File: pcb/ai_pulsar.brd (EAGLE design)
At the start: 30.5 x 30.5 mm, 24 parts, among them IC1 DS1307SO8-TIGHT, IC3 74HCT245MTC, J2 1X05, U1 MIC5205-3.3

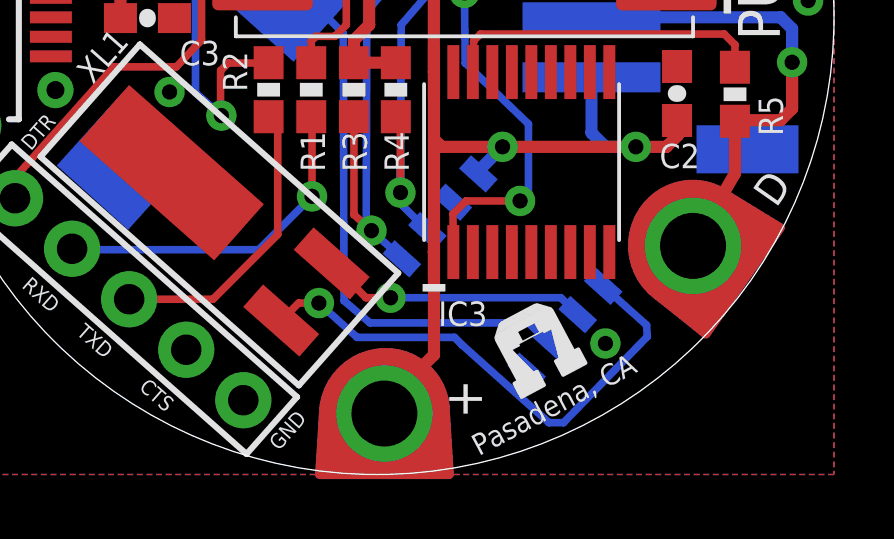
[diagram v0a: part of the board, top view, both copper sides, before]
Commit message: renamed a few parts
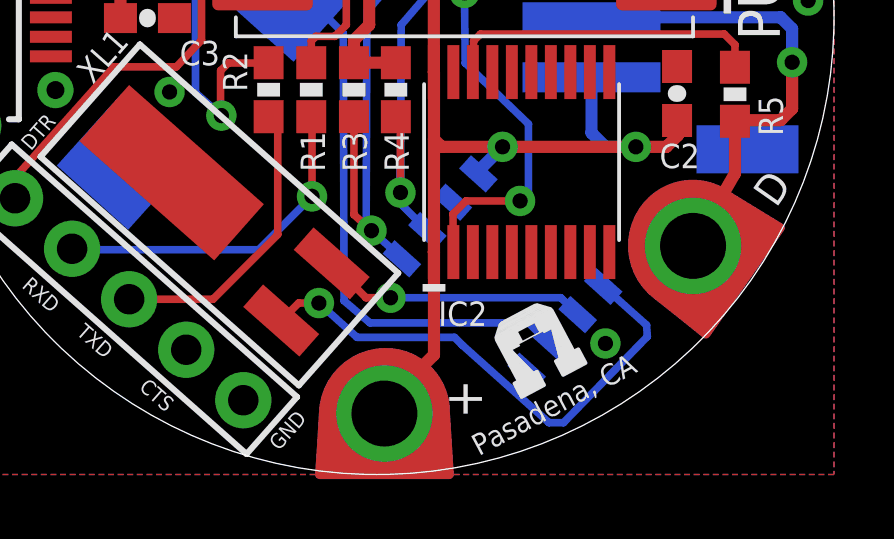
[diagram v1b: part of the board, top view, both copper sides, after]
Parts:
- C1: value 0.01uF -> 0.1uF
- renumbered IC3 to IC2
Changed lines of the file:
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@@
 <?xml version="1.0" encoding="utf-8"?>
 <!DOCTYPE eagle SYSTEM "eagle.dtd">
-<eagle version="7.1.0">
+<eagle version="7.0.0">
 <drawing>
 <settings>
@@
 <attribute name="NAME" x="10.1092" y="14.097" size="0.8128" layer="25" font="vector" ratio="10" rot="R270"/>
 </element>
-<element name="C1" library="Ai_Passives" package="CAP-0603" value="0.01uF" x="7.5946" y="18.0086" smashed="yes">
+<element name="C1" library="Ai_Passives" package="CAP-0603" value="0.1uF" x="7.5946" y="18.0086" smashed="yes">
 <attribute name="NAME" x="6.9596" y="18.7706" size="0.8128" layer="25" font="vector" ratio="10"/>
 </element>
-<element name="IC3" library="Ai_IC" package="SSOP20" value="74HCT245MTC" x="20.066" y="10.414" smashed="yes">
+<element name="IC2" library="Ai_IC" package="SSOP20" value="74HCT245MTC" x="20.066" y="10.414" smashed="yes">
 <attribute name="NAME" x="18.923" y="5.7658" size="0.8128" layer="25" font="vector" ratio="10" rot="R180"/>
 </element>
@@
 <contactref element="RFDUINO" pad="2"/>
 <contactref element="RFDUINO" pad="8"/>
-<contactref element="IC3" pad="10"/>
-<contactref element="IC3" pad="19"/>
+<contactref element="IC2" pad="10"/>
+<contactref element="IC2" pad="19"/>
 <contactref element="USB1" pad="GND"/>
 <contactref element="U1" pad="2"/>
@@
 <contactref element="+" pad="1"/>
 <contactref element="C2" pad="1"/>
-<contactref element="IC3" pad="20"/>
-<contactref element="IC3" pad="1"/>
+<contactref element="IC2" pad="20"/>
+<contactref element="IC2" pad="1"/>
 <contactref element="U1" pad="1"/>
 <contactref element="U1" pad="3"/>
@@
 <signal name="3V3IO2">
 <contactref element="RFDUINO" pad="3"/>
-<contactref element="IC3" pad="2"/>
+<contactref element="IC2" pad="2"/>
 <wire x1="17.791" y1="7.414" x2="17.78" y2="7.425" width="0.254" layer="1"/>
 <wire x1="17.78" y1="7.425" x2="17.78" y2="8.6868" width="0.254" layer="1"/>
@@
 </signal>
 <signal name="5VIO2">
-<contactref element="IC3" pad="18"/>
+<contactref element="IC2" pad="18"/>
 <contactref element="R5" pad="2"/>
 <wire x1="18.441" y1="13.414" x2="18.4658" y2="13.4388" width="0.254" layer="1"/>

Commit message: version 1.1. Fixed coin-cell polarity, added 5V on FTDI pins for easy programming
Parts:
- J1: value (none) -> JST-3-MALE; device Ai_Connectors:JSTP-3P-SMD -> Ai_Connectors:JST-3P-SMD
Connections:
- removed net CTS: J2.2
- removed net N$2: 3V-BATT.-, IC1.3
- new net N$1: 3V-BATT.+@1, 3V-BATT.+@2, IC1.3
- net 5V: now also J2.2
- net GND: now also 3V-BATT.-; no longer 3V-BATT.+$1, 3V-BATT.+$2
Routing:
- net N$2: track 18.9 -> 0.00 mm
- net N$1: track 0.00 -> 18.8 mm
- net 5V: track 49.5 -> 57.3 mm
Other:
- board text added: "5V"
- board text added: "v1.1"
- board text removed: "CTS"
- board text removed: "v1.0"
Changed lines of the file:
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@@
 <?xml version="1.0" encoding="utf-8"?>
 <!DOCTYPE eagle SYSTEM "eagle.dtd">
-<eagle version="7.0.0">
+<eagle version="7.1.0">
 <drawing>
 <settings>
@@
 <setting verticaltext="up"/>
 </settings>
-<grid distance="10" unitdist="mil" unit="mil" style="lines" multiple="1" display="yes" altdistance="0.025" altunitdist="inch" altunit="inch"/>
+<grid distance="5" unitdist="mil" unit="mil" style="lines" multiple="1" display="yes" altdistance="0.025" altunitdist="inch" altunit="inch"/>
 <layers>
 <layer number="1" name="Top" color="4" fill="1" visible="yes" active="yes"/>
@@
 <text x="17.653" y="3.175" size="1.27" layer="25" font="vector" ratio="10" rot="SR270">+</text>
 <text x="9.271" y="28.956" size="1.27" layer="25" font="vector" ratio="10" rot="SR180">-</text>
-<text x="29.8704" y="16.6624" size="0.7112" layer="25" font="vector" ratio="10" rot="R90">v1.0</text>
-<text x="3.7084" y="10.7696" size="0.508" layer="25" font="vector" ratio="10" rot="R48.5">DTR</text>
-<text x="4.7244" y="5.7404" size="0.508" layer="25" font="vector" ratio="10" rot="R138.5">RXD</text>
-<text x="6.5024" y="4.2164" size="0.508" layer="25" font="vector" ratio="10" rot="R138.5">TXD</text>
-<text x="8.5344" y="2.4384" size="0.508" layer="25" font="vector" ratio="10" rot="R138.5">CTS</text>
-<text x="12.5476" y="2.1844" size="0.508" layer="25" font="vector" ratio="10" rot="R228.5">GND</text>
+<text x="29.8704" y="16.6624" size="0.7112" layer="25" font="vector" ratio="10" rot="R90">v1.1</text>
+<text x="3.8354" y="10.5156" size="0.762" layer="25" font="vector" ratio="10" rot="R48.5">DTR</text>
+<text x="5.1054" y="5.4864" size="0.762" layer="25" font="vector" ratio="10" rot="R138.5">RXD</text>
+<text x="7.0104" y="3.8354" size="0.762" layer="25" font="vector" ratio="10" rot="R138.5">TXD</text>
+<text x="8.2804" y="2.6924" size="0.762" layer="25" font="vector" ratio="10" rot="R138.5">5V</text>
+<text x="12.8016" y="2.4384" size="0.762" layer="25" font="vector" ratio="10" rot="R228.5">GND</text>
 </plain>
 <attributes>
@@
 <attribute name="NAME" x="18.923" y="5.7658" size="0.8128" layer="25" font="vector" ratio="10" rot="R180"/>
 </element>
-<element name="3V-BATT" library="Ai_Connectors" package="CR1220-SMD" value="CR1220" x="12.319" y="16.51" smashed="yes" rot="MR312"/>
 <element name="IC1" library="Ai_IC" package="SO08-TIGHT" value="DS1307SO8-TIGHT" x="19.431" y="6.731" smashed="yes" rot="MR312">
 <attribute name="NAME" x="22.70684375" y="7.712009375" size="0.8128" layer="26" ratio="10" rot="MR42"/>
 </element>
-<element name="J1" library="Ai_Connectors" package="JSTP-3P-SMD" value="" x="25.0952" y="15.24" smashed="yes" rot="MR90"/>
+<element name="J1" library="Ai_Connectors" package="JST-3P-SMD" value="JST-3-MALE" x="25.0952" y="15.24" smashed="yes" rot="MR90"/>
 <element name="-" library="Ai_Connectors" package="1X01-PETAL" value="1X01-PETAL" x="6.985" y="25.4" smashed="yes" rot="R40"/>
 <element name="+" library="Ai_Connectors" package="1X01-PETAL" value="1X01-PETAL" x="15.494" y="2.032" smashed="yes" rot="R180"/>
@@
 <attribute name="NAME" x="7.62" y="20.32" size="0.8128" layer="25" font="vector" ratio="10" rot="R150"/>
 </element>
+<element name="3V-BATT" library="Ai_Connectors" package="CR1220-SMD" value="CR1220" x="12.319" y="16.51" smashed="yes" rot="MR312"/>
 </elements>
 <signals>
@@
 <contactref element="U1" pad="2"/>
 <contactref element="J1" pad="3"/>
-<contactref element="3V-BATT" pad="+$1"/>
-<contactref element="3V-BATT" pad="+$2"/>
 <contactref element="J2" pad="1"/>
 <contactref element="IC1" pad="4"/>
@@
 <via x="8.3312" y="12.7508" extent="1-16" drill="0.508"/>
 <via x="22.86" y="4.3688" extent="1-16" drill="0.508"/>
+<contactref element="3V-BATT" pad="-"/>
 </signal>
 <signal name="N$9">
@@
 <wire x1="16.002" y1="19.9136" x2="17.141" y2="18.7746" width="0.4064" layer="1"/>
 <wire x1="17.141" y1="18.7746" x2="17.141" y2="13.414" width="0.4064" layer="1"/>
+<contactref element="J2" pad="2"/>
+<wire x1="8.887346875" y1="4.15894375" x2="12.192" y2="4.953" width="0.4064" layer="16"/>
+<wire x1="12.192" y1="4.953" x2="15.494" y2="2.032" width="0.4064" layer="16"/>
 </signal>
 <signal name="3V3" class="1">
@@
 <wire x1="27.2144" y1="11.811" x2="27.178" y2="11.7746" width="0.4064" layer="1"/>
 </signal>
-<signal name="N$2">
-<contactref element="IC1" pad="3"/>
-<contactref element="3V-BATT" pad="-"/>
-<wire x1="12.319" y1="16.51" x2="14.1224" y2="14.7066" width="0.254" layer="16"/>
-<wire x1="14.1224" y1="14.7066" x2="14.1478" y2="5.7912" width="0.254" layer="16"/>
-<wire x1="14.1478" y1="5.7912" x2="15.0114" y2="5.0546" width="0.254" layer="16"/>
-<wire x1="15.0114" y1="5.0546" x2="20.2946" y2="5.0546" width="0.254" layer="16"/>
-<wire x1="20.2946" y1="5.0546" x2="20.989065625" y2="4.385534375" width="0.254" layer="16"/>
-<wire x1="20.989065625" y1="4.385534375" x2="21.086909375" y2="4.385534375" width="0.254" layer="16"/>
-</signal>
-<signal name="CTS">
-<contactref element="J2" pad="2"/>
-</signal>
 <signal name="TXO">
 <contactref element="J2" pad="3"/>
@@
 <wire x1="6.8009125" y1="21.569" x2="6.477" y2="21.082" width="0.4064" layer="1"/>
 </signal>
+<signal name="N$1">
+<contactref element="IC1" pad="3"/>
+<wire x1="21.086909375" y1="4.385534375" x2="20.4216" y2="5.0292" width="0.254" layer="16"/>
+<wire x1="20.4216" y1="5.0292" x2="15.2654" y2="5.0546" width="0.254" layer="16"/>
+<wire x1="14.097" y1="9.652" x2="14.097" y2="6.096" width="0.254" layer="16"/>
+<wire x1="14.097" y1="6.096" x2="15.2654" y2="5.0546" width="0.254" layer="16"/>
+<contactref element="3V-BATT" pad="+@2"/>
+<wire x1="14.097" y1="9.652" x2="13.335" y2="10.414" width="0.254" layer="16"/>
+<wire x1="13.335" y1="10.414" x2="6.83213125" y2="10.416209375" width="0.254" layer="16"/>
+<contactref element="3V-BATT" pad="+@1"/>
+<wire x1="13.335" y1="10.414" x2="17.805871875" y2="22.6037875" width="0" layer="19" extent="16-16"/>
+</signal>
 </signals>
